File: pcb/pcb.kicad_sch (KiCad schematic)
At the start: 0 parts

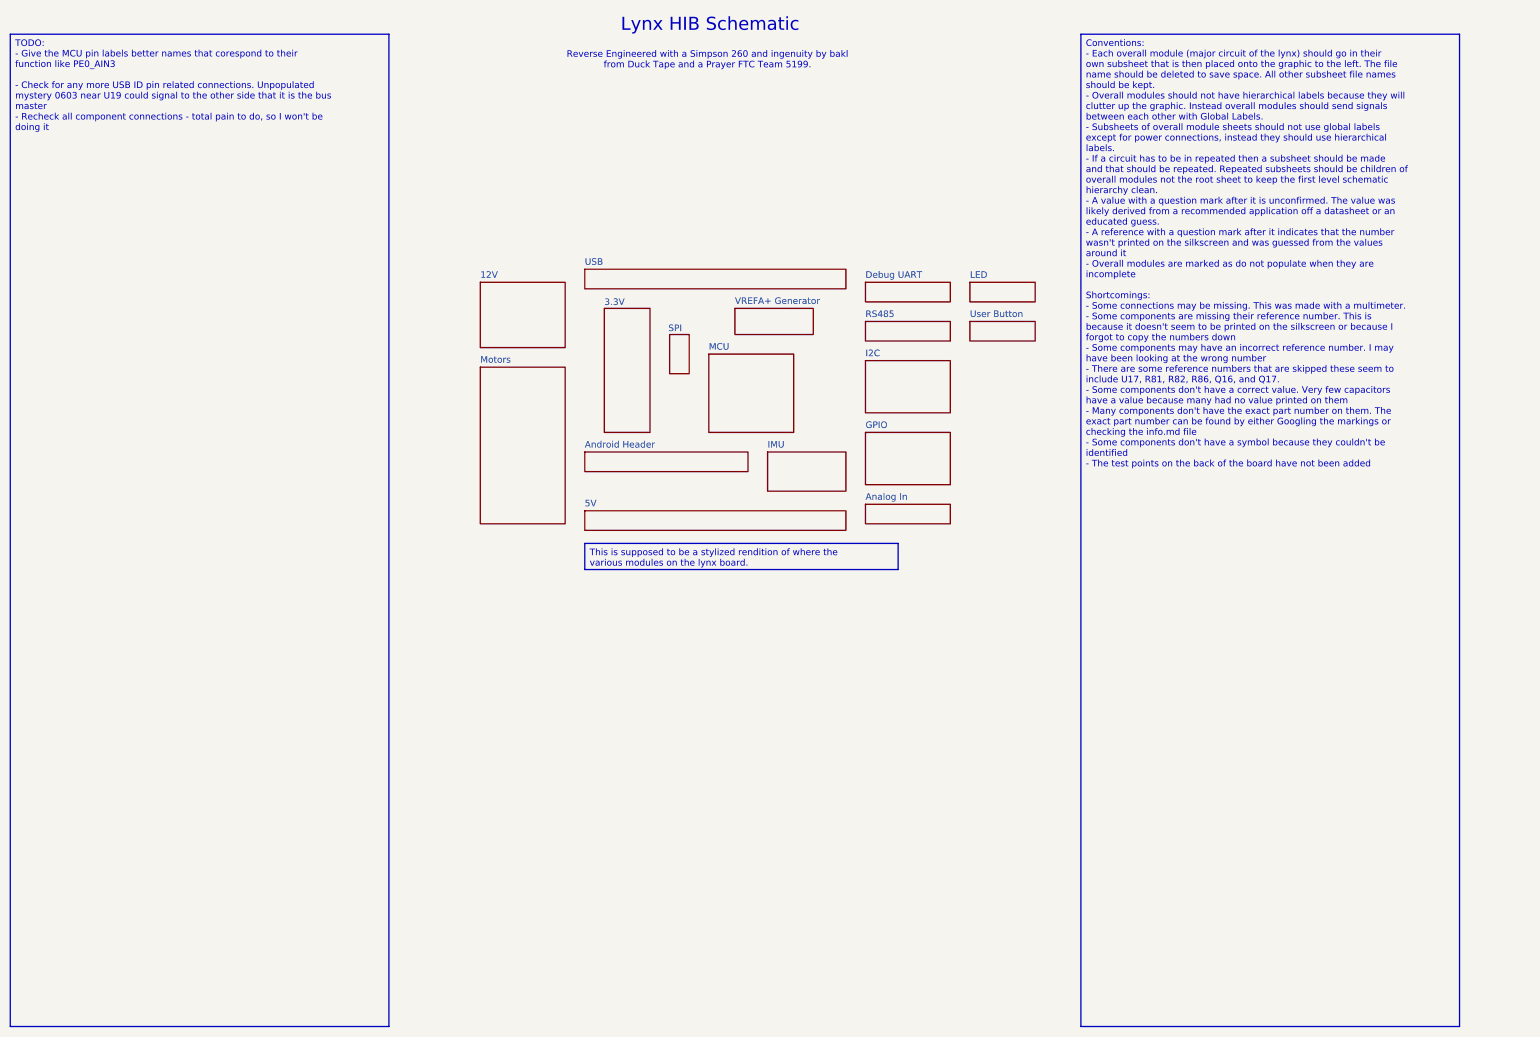
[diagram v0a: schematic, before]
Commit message: Add the last few mystery components to the schematic, update the licence and start on RHSP
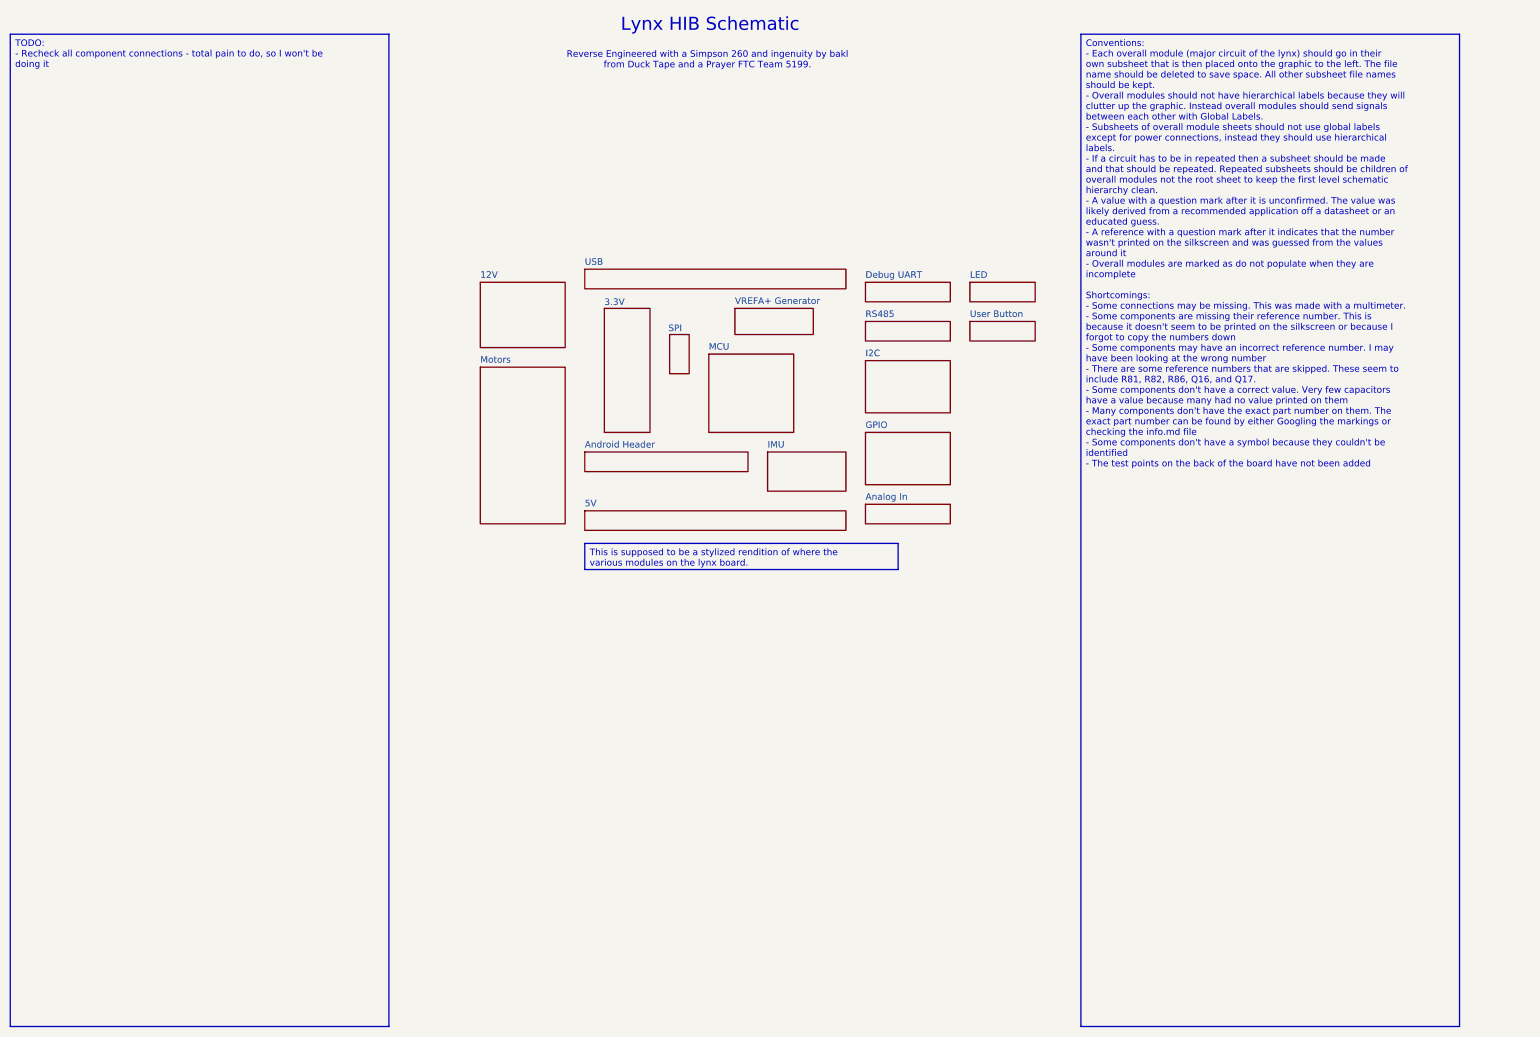
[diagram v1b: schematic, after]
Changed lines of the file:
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@@
 		)
 	)
-	(text_box "TODO:\n - Give the MCU pin labels better names that corespond to their function like PE0_AIN3\n\n - Check for any more USB ID pin related connections. Unpopulated mystery 0603 near U19 could signal to the other side that it is the bus master\n - Recheck all component connections - total pain to do, so I won't be doing it\n \n \n"
+	(text_box "TODO:\n - Recheck all component connections - total pain to do, so I won't be doing it\n \n \n"
 		(exclude_from_sim no)
 		(at 7.62 7.62 0)
@@
 		)
 	)
-	(text_box "Conventions:\n - Each overall module (major circuit of the lynx) should go in their own subsheet that is then placed onto the graphic to the left. The file name should be deleted to save space. All other subsheet file names should be kept.\n - Overall modules should not have hierarchical labels because they will clutter up the graphic. Instead overall modules should send signals between each other with Global Labels.\n - Subsheets of overall module sheets should not use global labels except for power connections, instead they should use hierarchical labels.\n - If a circuit has to be in repeated then a subsheet should be made and that should be repeated. Repeated subsheets should be children of overall modules not the root sheet to keep the first level schematic hierarchy clean.\n - A value with a question mark after it is unconfirmed. The value was likely derived from a recommended application off a datasheet or an educated guess.\n - A reference with a question mark after it indicates that the number wasn't printed on the silkscreen and was guessed from the values around it\n - Overall modules are marked as do not populate when they are incomplete\n\nShortcomings:\n - Some connections may be missing. This was made with a multimeter.\n - Some components are missing their reference number. This is because it doesn't seem to be printed on the silkscreen or because I forgot to copy the numbers down\n - Some components may have an incorrect reference number. I may have been looking at the wrong number\n - There are some reference numbers that are skipped these seem to include U17, R81, R82, R86, Q16, and Q17.\n - Some components don't have a correct value. Very few capacitors have a value because many had no value printed on them\n - Many components don't have the exact part number on them. The exact part number can be found by either Googling the markings or checking the info.md file\n - Some components don't have a symbol because they couldn't be identified\n - The test points on the back of the board have not been added\n "
+	(text_box "Conventions:\n - Each overall module (major circuit of the lynx) should go in their own subsheet that is then placed onto the graphic to the left. The file name should be deleted to save space. All other subsheet file names should be kept.\n - Overall modules should not have hierarchical labels because they will clutter up the graphic. Instead overall modules should send signals between each other with Global Labels.\n - Subsheets of overall module sheets should not use global labels except for power connections, instead they should use hierarchical labels.\n - If a circuit has to be in repeated then a subsheet should be made and that should be repeated. Repeated subsheets should be children of overall modules not the root sheet to keep the first level schematic hierarchy clean.\n - A value with a question mark after it is unconfirmed. The value was likely derived from a recommended application off a datasheet or an educated guess.\n - A reference with a question mark after it indicates that the number wasn't printed on the silkscreen and was guessed from the values around it\n - Overall modules are marked as do not populate when they are incomplete\n\nShortcomings:\n - Some connections may be missing. This was made with a multimeter.\n - Some components are missing their reference number. This is because it doesn't seem to be printed on the silkscreen or because I forgot to copy the numbers down\n - Some components may have an incorrect reference number. I may have been looking at the wrong number\n - There are some reference numbers that are skipped. These seem to include R81, R82, R86, Q16, and Q17.\n - Some components don't have a correct value. Very few capacitors have a value because many had no value printed on them\n - Many components don't have the exact part number on them. The exact part number can be found by either Googling the markings or checking the info.md file\n - Some components don't have a symbol because they couldn't be identified\n - The test points on the back of the board have not been added\n "
 		(exclude_from_sim no)
 		(at 215.9 7.62 0)

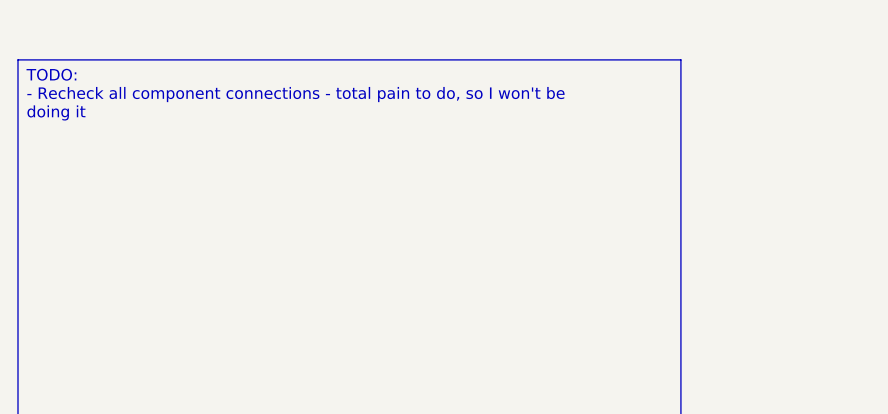
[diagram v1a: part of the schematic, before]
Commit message: Add hardware encoder support
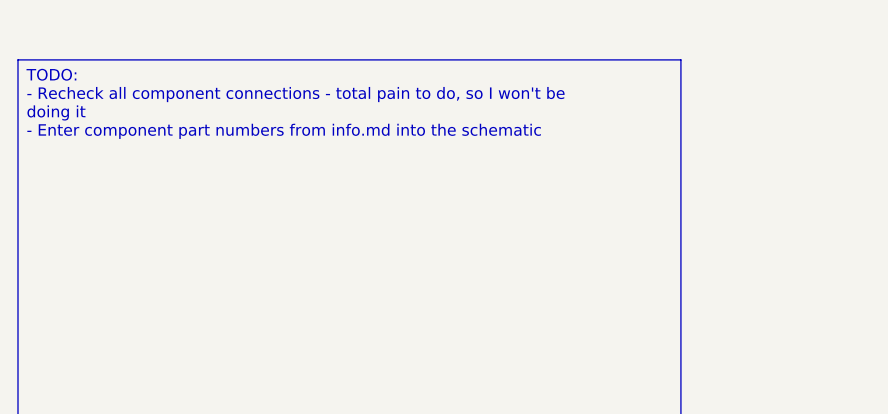
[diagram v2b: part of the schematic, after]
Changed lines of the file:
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@@
 		)
 	)
-	(text_box "TODO:\n - Recheck all component connections - total pain to do, so I won't be doing it\n \n \n"
+	(text_box "TODO:\n - Recheck all component connections - total pain to do, so I won't be doing it\n - Enter component part numbers from info.md into the schematic\n \n \n"
 		(exclude_from_sim no)
 		(at 7.62 7.62 0)
